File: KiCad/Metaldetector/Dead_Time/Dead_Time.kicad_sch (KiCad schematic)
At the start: 18 parts, among them Q7 PNP_BC558, U1 L272M, U2 74AUC2G04

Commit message: ændret kicad opsætning
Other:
- moved on the sheet: 5V_pin2, C3, GND_pin2, On_Off1, PWM_1, PWM_1_NOT2, PWM_2, PWM_2_NOT2, PWM_In1, Q7, R10, R11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

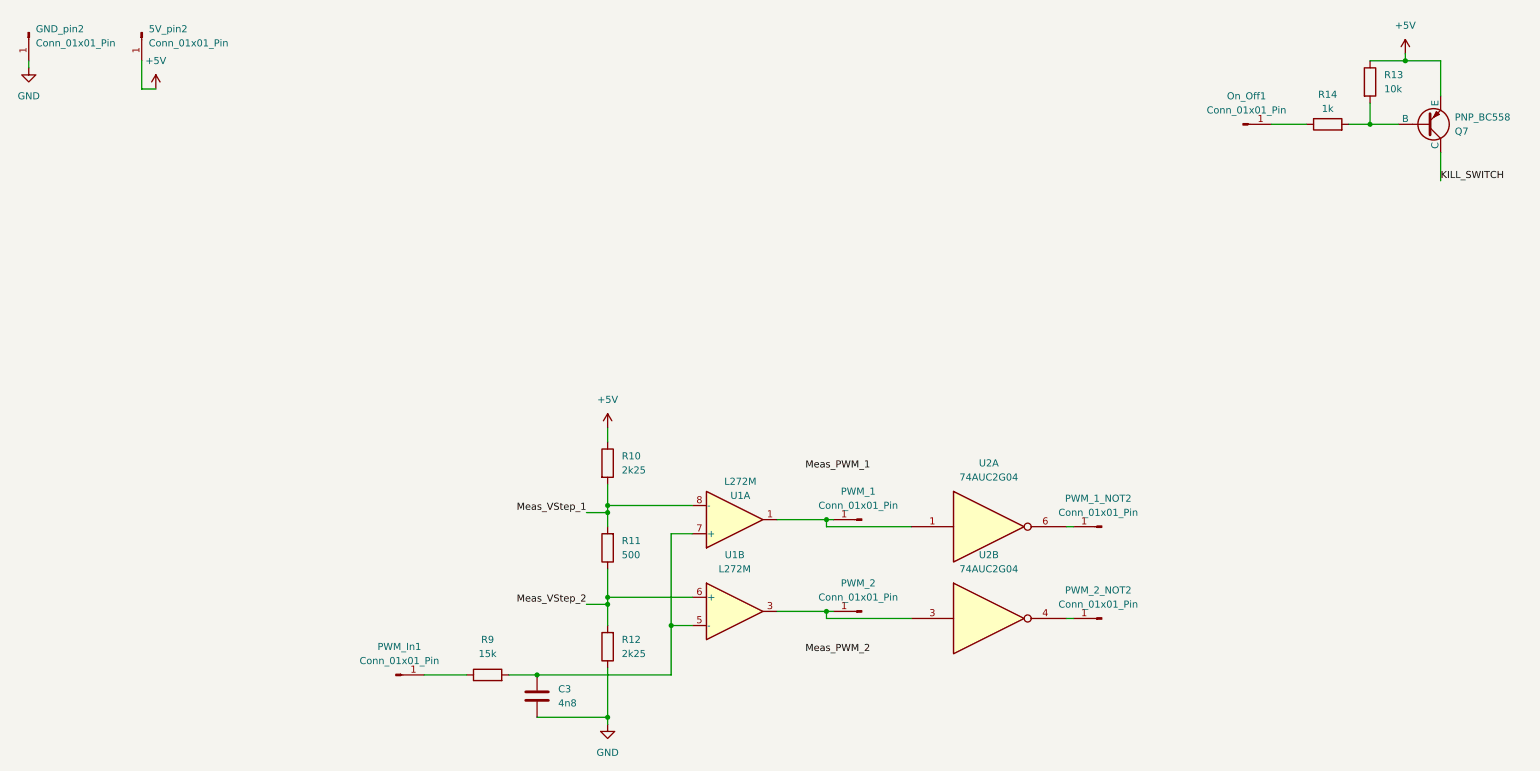
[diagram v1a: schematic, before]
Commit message: nyste pcb design til AP forstærker
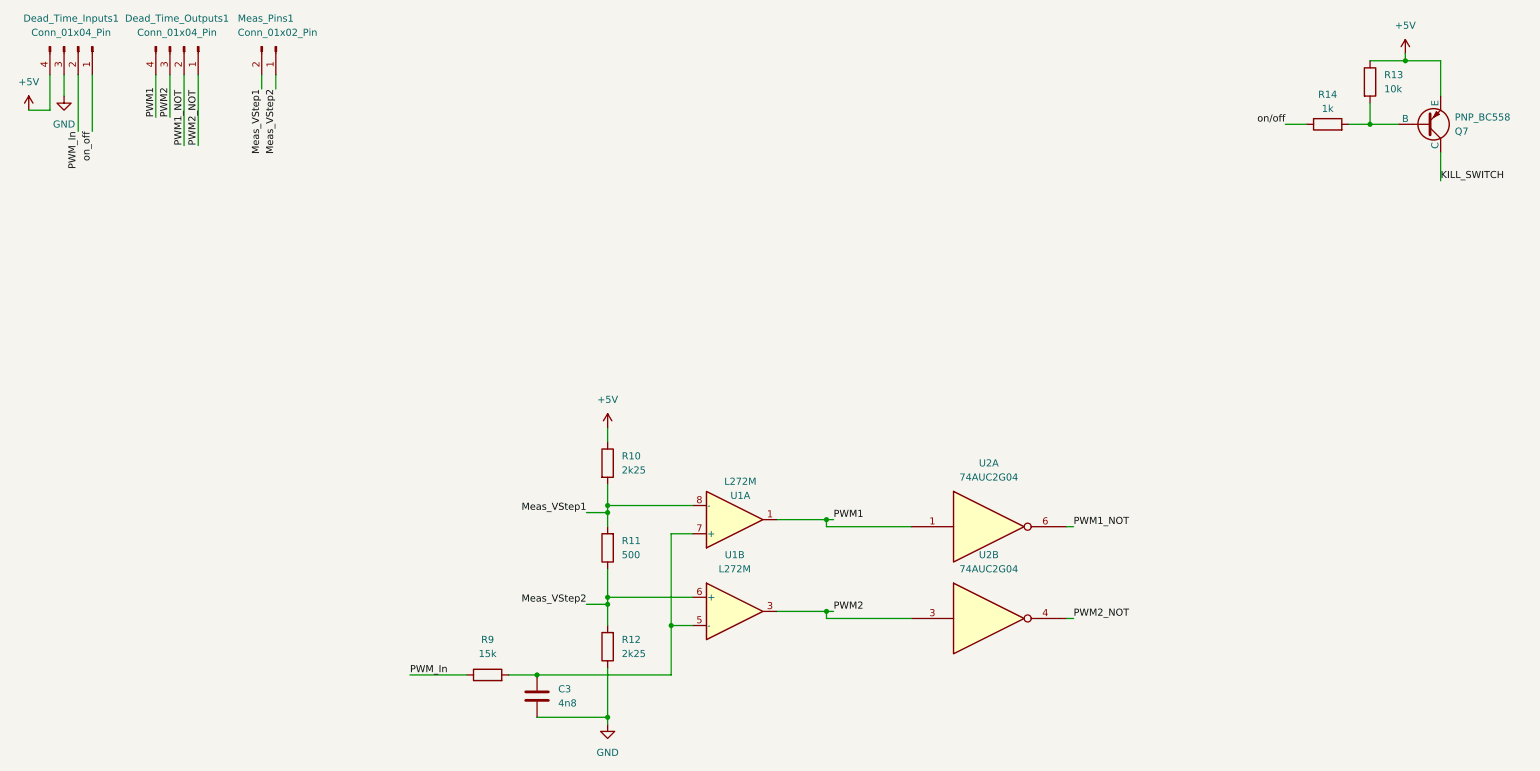
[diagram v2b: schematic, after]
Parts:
- removed 5V_pin2, GND_pin2, On_Off1, PWM_1, PWM_1_NOT2, PWM_2, PWM_2_NOT2, PWM_In1: Conn_01x01_Pin, symbol Connector:Conn_01x01_Pin
- added Dead_Time_Inputs1, Dead_Time_Outputs1: Conn_01x04_Pin, Connector_PinHeader_2.54mm:PinHeader_1x04_P2.54mm_Horizontal, symbol Connector:Conn_01x04_Pin
- added Meas_Pins1: Conn_01x02_Pin, Connector_PinHeader_2.54mm:PinHeader_1x02_P2.54mm_Vertical, symbol Connector:Conn_01x02_Pin
- C3: footprint (none) -> Capacitor_THT:C_Rect_L7.0mm_W2.5mm_P5.00mm
- Q7: footprint (none) -> Package_TO_SOT_THT:TO-92_Inline
- R10, R11, R12, R13, R14, R9: footprint (none) -> Resistor_THT:R_Axial_DIN0204_L3.6mm_D1.6mm_P5.08mm_Horizontal
- U2: footprint (none) -> Package_DIP:DIP-14_W7.62mm
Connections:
- net +5V: now also Dead_Time_Inputs1.4 (Pin_4)
- net GND: now also Dead_Time_Inputs1.3 (Pin_3)
- net PWM1: now reaches U1.1, U2.1
- net PWM1: now also Dead_Time_Outputs1.4 (Pin_4)
- net PWM_In: now reaches R9.1
- net PWM_In: now also Dead_Time_Inputs1.2 (Pin_2)
- net PWM2: now reaches U1.3, U2.3
- net PWM2: now also Dead_Time_Outputs1.3 (Pin_3)
- net PWM1_NOT: now reaches U2.6
- net PWM1_NOT: now also Dead_Time_Outputs1.2 (Pin_2)
- net on/off: now reaches R14.1
- net PWM2_NOT: now reaches U2.4
- net PWM2_NOT: now also Dead_Time_Outputs1.1 (Pin_1)
- net Meas_VStep_1 renamed Meas_VStep1
- net Meas_VStep1: now also Meas_Pins1.2 (Pin_2)
- net Meas_VStep_2 renamed Meas_VStep2
- net Meas_VStep2: now also Meas_Pins1.1 (Pin_1)
- new net on_off: Dead_Time_Inputs1.1 (Pin_1)
